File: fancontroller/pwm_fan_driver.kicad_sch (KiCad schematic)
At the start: 4 parts, among them M5 FAN0, Q11 AO3400A, Q12 AO3401A

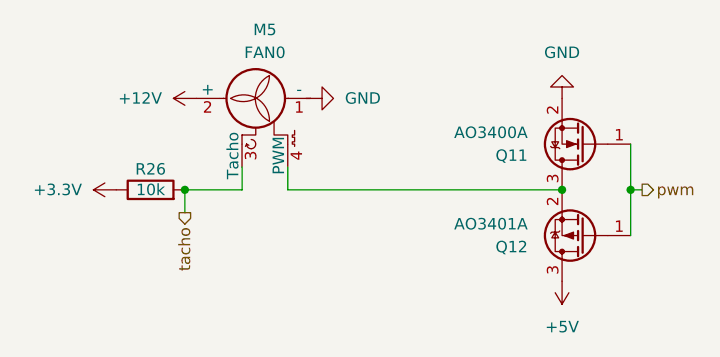
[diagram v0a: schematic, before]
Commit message: Improve footprints and do massive overhaul for part numbering for better future order
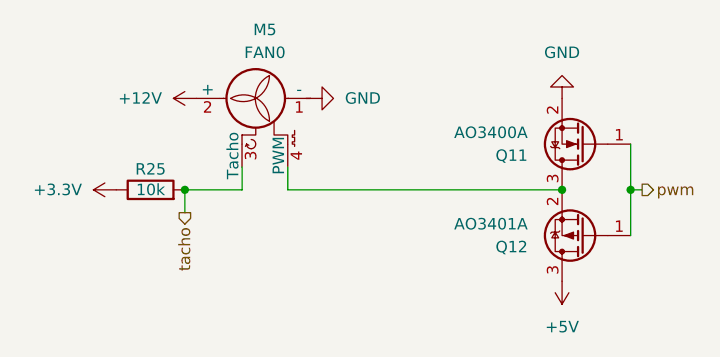
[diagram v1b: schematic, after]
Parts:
- renumbered R26 to R25
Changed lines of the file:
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@@
 		(dnp no)
 		(fields_autoplaced yes)
-		(property "Reference" "#PWR053"
+		(property "Reference" "#PWR055"
 			(at 76.2 55.88 0)
 			(effects
@@
 			(project "fancontroller"
 				(path "/0224fd83-71fd-467a-bea0-55e2843206f4/4781c691-5627-48f1-a43d-9e593546ee46"
-					(reference "#PWR053")
+					(reference "#PWR055")
 					(unit 1)
 				)
 				(path "/0224fd83-71fd-467a-bea0-55e2843206f4/60b0bd1c-d5e0-4612-ac2f-d2d398cb3c41"
-					(reference "#PWR048")
+					(reference "#PWR050")
 					(unit 1)
 				)
 				(path "/0224fd83-71fd-467a-bea0-55e2843206f4/697a23fd-1c55-47ba-b721-989bf051367e"
-					(reference "#PWR033")
+					(reference "#PWR035")
 					(unit 1)
 				)
 				(path "/0224fd83-71fd-467a-bea0-55e2843206f4/b7451969-b5c8-4a59-be86-9c30f199506d"
-					(reference "#PWR058")
+					(reference "#PWR060")
 					(unit 1)
 				)
 				(path "/0224fd83-71fd-467a-bea0-55e2843206f4/b7f12c5b-539e-4b68-ad77-d041234edbdf"
-					(reference "#PWR043")
+					(reference "#PWR045")
 					(unit 1)
 				)
 				(path "/0224fd83-71fd-467a-bea0-55e2843206f4/d4b2e9bb-c9e1-4011-9754-18f52765a82d"
-					(reference "#PWR038")
+					(reference "#PWR040")
 					(unit 1)
 				)
@@
 		(dnp no)
 		(fields_autoplaced yes)
-		(property "Reference" "#PWR054"
+		(property "Reference" "#PWR056"
 			(at 91.44 55.88 0)
 			(effects
@@
 			(project "fancontroller"
 				(path "/0224fd83-71fd-467a-bea0-55e2843206f4/4781c691-5627-48f1-a43d-9e593546ee46"
-					(reference "#PWR054")
+					(reference "#PWR056")
 					(unit 1)
 				)
 				(path "/0224fd83-71fd-467a-bea0-55e2843206f4/60b0bd1c-d5e0-4612-ac2f-d2d398cb3c41"
-					(reference "#PWR049")
+					(reference "#PWR051")
 					(unit 1)
 				)
 				(path "/0224fd83-71fd-467a-bea0-55e2843206f4/697a23fd-1c55-47ba-b721-989bf051367e"
-					(reference "#PWR034")
+					(reference "#PWR036")
 					(unit 1)
 				)
 				(path "/0224fd83-71fd-467a-bea0-55e2843206f4/b7451969-b5c8-4a59-be86-9c30f199506d"
-					(reference "#PWR059")
+					(reference "#PWR061")
 					(unit 1)
 				)
 				(path "/0224fd83-71fd-467a-bea0-55e2843206f4/b7f12c5b-539e-4b68-ad77-d041234edbdf"
-					(reference "#PWR044")
+					(reference "#PWR046")
 					(unit 1)
 				)
 				(path "/0224fd83-71fd-467a-bea0-55e2843206f4/d4b2e9bb-c9e1-4011-9754-18f52765a82d"
-					(reference "#PWR039")
+					(reference "#PWR041")
 					(unit 1)
 				)
@@
 			)
 		)
+		(property "Power" ""
+			(at 115.57 60.96 0)
+			(effects
+				(font
+					(size 1.27 1.27)
+				)
+				(hide yes)
+			)
+		)
 		(pin "1"
 		)
@@
 			)
 		)
+		(property "Power" ""
+			(at 80.01 55.88 0)
+			(effects
+				(font
+					(size 1.27 1.27)
+				)
+				(hide yes)
+			)
+		)
 		(pin "4"
 		)
@@
 		(dnp no)
 		(fields_autoplaced yes)
-		(property "Reference" "#PWR056"
+		(property "Reference" "#PWR058"
 			(at 113.03 72.39 0)
 			(effects
@@
 			(project "fancontroller"
 				(path "/0224fd83-71fd-467a-bea0-55e2843206f4/4781c691-5627-48f1-a43d-9e593546ee46"
-					(reference "#PWR056")
+					(reference "#PWR058")
 					(unit 1)
 				)
 				(path "/0224fd83-71fd-467a-bea0-55e2843206f4/60b0bd1c-d5e0-4612-ac2f-d2d398cb3c41"
-					(reference "#PWR051")
+					(reference "#PWR053")
 					(unit 1)
 				)
 				(path "/0224fd83-71fd-467a-bea0-55e2843206f4/697a23fd-1c55-47ba-b721-989bf051367e"
-					(reference "#PWR036")
+					(reference "#PWR038")
 					(unit 1)
 				)
 				(path "/0224fd83-71fd-467a-bea0-55e2843206f4/b7451969-b5c8-4a59-be86-9c30f199506d"
-					(reference "#PWR061")
+					(reference "#PWR063")
 					(unit 1)
 				)
 				(path "/0224fd83-71fd-467a-bea0-55e2843206f4/b7f12c5b-539e-4b68-ad77-d041234edbdf"
-					(reference "#PWR046")
+					(reference "#PWR048")
 					(unit 1)
 				)
 				(path "/0224fd83-71fd-467a-bea0-55e2843206f4/d4b2e9bb-c9e1-4011-9754-18f52765a82d"
-					(reference "#PWR041")
+					(reference "#PWR043")
 					(unit 1)
 				)
@@
 		(dnp no)
 		(fields_autoplaced yes)
-		(property "Reference" "#PWR055"
+		(property "Reference" "#PWR057"
 			(at 113.03 49.53 0)
 			(effects
@@
 			(project "fancontroller"
 				(path "/0224fd83-71fd-467a-bea0-55e2843206f4/4781c691-5627-48f1-a43d-9e593546ee46"
-					(reference "#PWR055")
+					(reference "#PWR057")
 					(unit 1)
 				)
 				(path "/0224fd83-71fd-467a-bea0-55e2843206f4/60b0bd1c-d5e0-4612-ac2f-d2d398cb3c41"
-					(reference "#PWR050")
+					(reference "#PWR052")
 					(unit 1)
 				)
 				(path "/0224fd83-71fd-467a-bea0-55e2843206f4/697a23fd-1c55-47ba-b721-989bf051367e"
-					(reference "#PWR035")
+					(reference "#PWR037")
 					(unit 1)
 				)
 				(path "/0224fd83-71fd-467a-bea0-55e2843206f4/b7451969-b5c8-4a59-be86-9c30f199506d"
-					(reference "#PWR060")
+					(reference "#PWR062")
 					(unit 1)
 				)
 				(path "/0224fd83-71fd-467a-bea0-55e2843206f4/b7f12c5b-539e-4b68-ad77-d041234edbdf"
-					(reference "#PWR045")
+					(reference "#PWR047")
 					(unit 1)
 				)
 				(path "/0224fd83-71fd-467a-bea0-55e2843206f4/d4b2e9bb-c9e1-4011-9754-18f52765a82d"
-					(reference "#PWR040")
+					(reference "#PWR042")
 					(unit 1)
 				)
@@
 		(dnp no)
 		(fields_autoplaced yes)
-		(property "Reference" "#PWR052"
+		(property "Reference" "#PWR054"
 			(at 67.31 66.04 0)
 			(effects
@@
 			(project ""
 				(path "/0224fd83-71fd-467a-bea0-55e2843206f4/4781c691-5627-48f1-a43d-9e593546ee46"
-					(reference "#PWR052")
+					(reference "#PWR054")
 					(unit 1)
 				)
 				(path "/0224fd83-71fd-467a-bea0-55e2843206f4/60b0bd1c-d5e0-4612-ac2f-d2d398cb3c41"
-					(reference "#PWR047")
+					(reference "#PWR049")
 					(unit 1)
 				)
 				(path "/0224fd83-71fd-467a-bea0-55e2843206f4/697a23fd-1c55-47ba-b721-989bf051367e"
-					(reference "#PWR032")
+					(reference "#PWR034")
 					(unit 1)
 				)
 				(path "/0224fd83-71fd-467a-bea0-55e2843206f4/b7451969-b5c8-4a59-be86-9c30f199506d"
-					(reference "#PWR057")
+					(reference "#PWR059")
 					(unit 1)
 				)
 				(path "/0224fd83-71fd-467a-bea0-55e2843206f4/b7f12c5b-539e-4b68-ad77-d041234edbdf"
-					(reference "#PWR042")
+					(reference "#PWR044")
 					(unit 1)
 				)
 				(path "/0224fd83-71fd-467a-bea0-55e2843206f4/d4b2e9bb-c9e1-4011-9754-18f52765a82d"
-					(reference "#PWR037")
+					(reference "#PWR039")
 					(unit 1)
 				)
@@
 		(on_board yes)
 		(dnp no)
-		(property "Reference" "R26"
+		(property "Reference" "R25"
 			(at 67.31 63.754 90)
 			(effects
@@
 		)
 		(property "JLCPCB Rotation Offset" ""
+			(at 67.31 66.04 0)
+			(effects
+				(font
+					(size 1.27 1.27)
+				)
+				(hide yes)
+			)
+		)
+		(property "Power" ""
 			(at 67.31 66.04 0)
 			(effects
@@
 			(project "fancontroller"
 				(path "/0224fd83-71fd-467a-bea0-55e2843206f4/4781c691-5627-48f1-a43d-9e593546ee46"
+					(reference "R25")
+					(unit 1)
+				)
+				(path "/0224fd83-71fd-467a-bea0-55e2843206f4/60b0bd1c-d5e0-4612-ac2f-d2d398cb3c41"
+					(reference "R24")
+					(unit 1)
+				)
+				(path "/0224fd83-71fd-467a-bea0-55e2843206f4/697a23fd-1c55-47ba-b721-989bf051367e"
+					(reference "R21")
+					(unit 1)
+				)
+				(path "/0224fd83-71fd-467a-bea0-55e2843206f4/b7451969-b5c8-4a59-be86-9c30f199506d"
 					(reference "R26")
 					(unit 1)
 				)
-				(path "/0224fd83-71fd-467a-bea0-55e2843206f4/60b0bd1c-d5e0-4612-ac2f-d2d398cb3c41"
-					(reference "R25")
-					(unit 1)
-				)
-				(path "/0224fd83-71fd-467a-bea0-55e2843206f4/697a23fd-1c55-47ba-b721-989bf051367e"
+				(path "/0224fd83-71fd-467a-bea0-55e2843206f4/b7f12c5b-539e-4b68-ad77-d041234edbdf"
+					(reference "R23")
+					(unit 1)
+				)
+				(path "/0224fd83-71fd-467a-bea0-55e2843206f4/d4b2e9bb-c9e1-4011-9754-18f52765a82d"
 					(reference "R22")
-					(unit 1)
-				)
-				(path "/0224fd83-71fd-467a-bea0-55e2843206f4/b7451969-b5c8-4a59-be86-9c30f199506d"
-					(reference "R27")
-					(unit 1)
-				)
-				(path "/0224fd83-71fd-467a-bea0-55e2843206f4/b7f12c5b-539e-4b68-ad77-d041234edbdf"
-					(reference "R24")
-					(unit 1)
-				)
-				(path "/0224fd83-71fd-467a-bea0-55e2843206f4/d4b2e9bb-c9e1-4011-9754-18f52765a82d"
-					(reference "R23")
 					(unit 1)
 				)
@@
 			(at 115.57 71.12 0)
 			(effects
+				(font
+					(size 1.27 1.27)
+				)
+				(hide yes)
+			)
+		)
+		(property "Power" ""
+			(at 115.57 71.12 0)
+			(effects
